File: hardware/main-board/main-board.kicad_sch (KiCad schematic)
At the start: 87 parts, among them J1 USB_C_Receptacle_USB2.0, J2 DNI, J3 Display Connector, J4 Conn_01x02, SW1 SW_Push, SW2 SW_Push, SW3 SW_Push, SW4 SW_Push, SW5 SW_Detect, SW6 SW_Boot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

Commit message: Various minor PCB fixups
Changed C1 footprint from an 0402 resistor to an 0402 capacitor. This
change shoulds be metadata only, or close to it, but makes the BOM data
less confusing.

Updated PCB metadata from schematic, which should pull in all of the BOM
manufacturer/vendor changes that were made when procuring components for
the production run.  It should also pull in any net name changes due to
KiCad updates.
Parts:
- C1: footprint Resistor_SMD:R_0402_1005Metric -> Capacitor_SMD:C_0402_1005Metric
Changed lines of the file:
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@@
     (property "Reference" "C1" (id 0) (at 27.94 24.6634 90))
     (property "Value" "1uF" (id 1) (at 27.94 26.9748 90))
-    (property "Footprint" "Resistor_SMD:R_0402_1005Metric" (id 2) (at 27.94 30.48 0)
+    (property "Footprint" "Capacitor_SMD:C_0402_1005Metric" (id 2) (at 27.94 30.48 0)
       (effects (font (size 1.27 1.27)) hide)
     )
@@
     )
     (path "/00000000-0000-0000-0000-00006056d7c9"
-      (reference "C1") (unit 1) (value "1uF") (footprint "Resistor_SMD:R_0402_1005Metric")
+      (reference "C1") (unit 1) (value "1uF") (footprint "Capacitor_SMD:C_0402_1005Metric")
     )
     (path "/00000000-0000-0000-0000-0000605786b2"

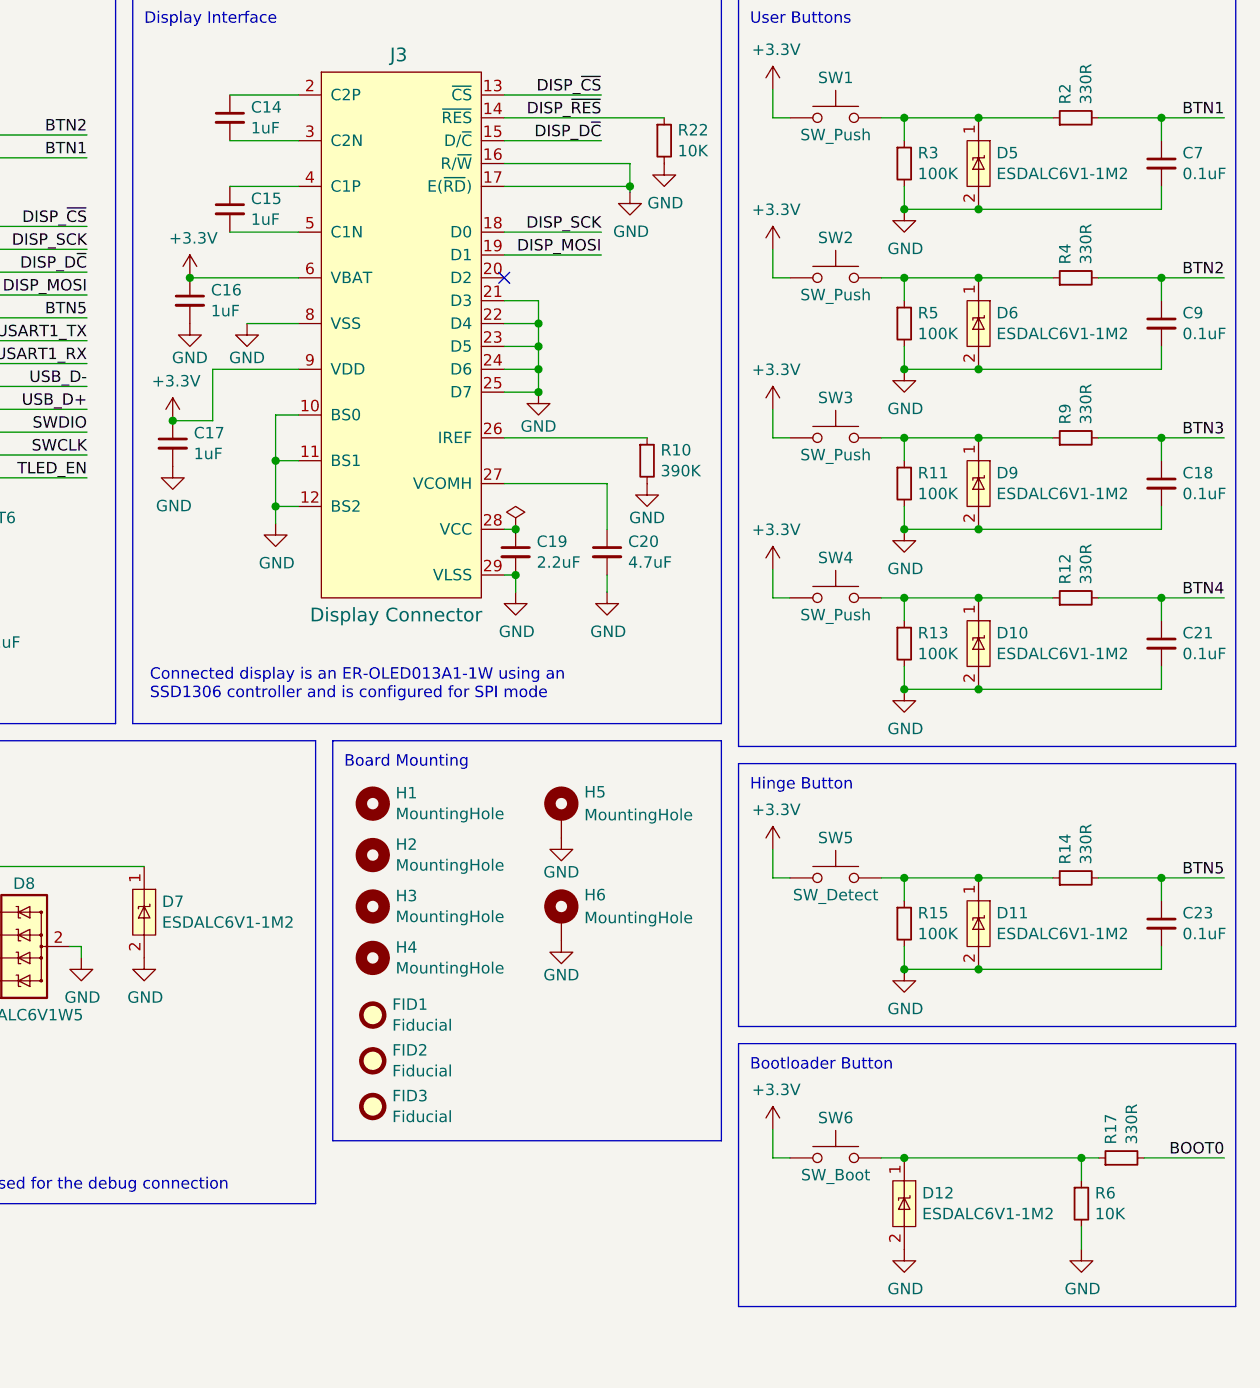
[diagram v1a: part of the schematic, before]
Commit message: Switch all single-line TVS diodes to the Semtech uClamp3301H
The ST diodes used in the original design had two main problems:
- Their package size made handling and manufacturability difficult,
  resulting in a lot of spotted issues on production boards
- Their rating can only protect 5V-tolerant lines, and a few of the
  buttons are actually connected on MCU pins that may only be 3.3V
  tolerant

This changes all of these diodes to a Semtech diode that's in a
larger and easier to handle package, which is also designed for
protecting 3.3V lines. Care was taken to minimize any and all changes
not strictly necessary for changing this one part, in an effort to
preserve the validity of existing EMC certification. That being said,
the only arcing ever seen during that testing was to the shield of the
USB connector, which is handled by completely unrelated protection
components.

If it is later determined that a TVS diode with a 5V working voltage is
more appropriate, Semtech also makes the uClamp0501H which is in an
identical package and can be a drop-in alternative.

Fix #41
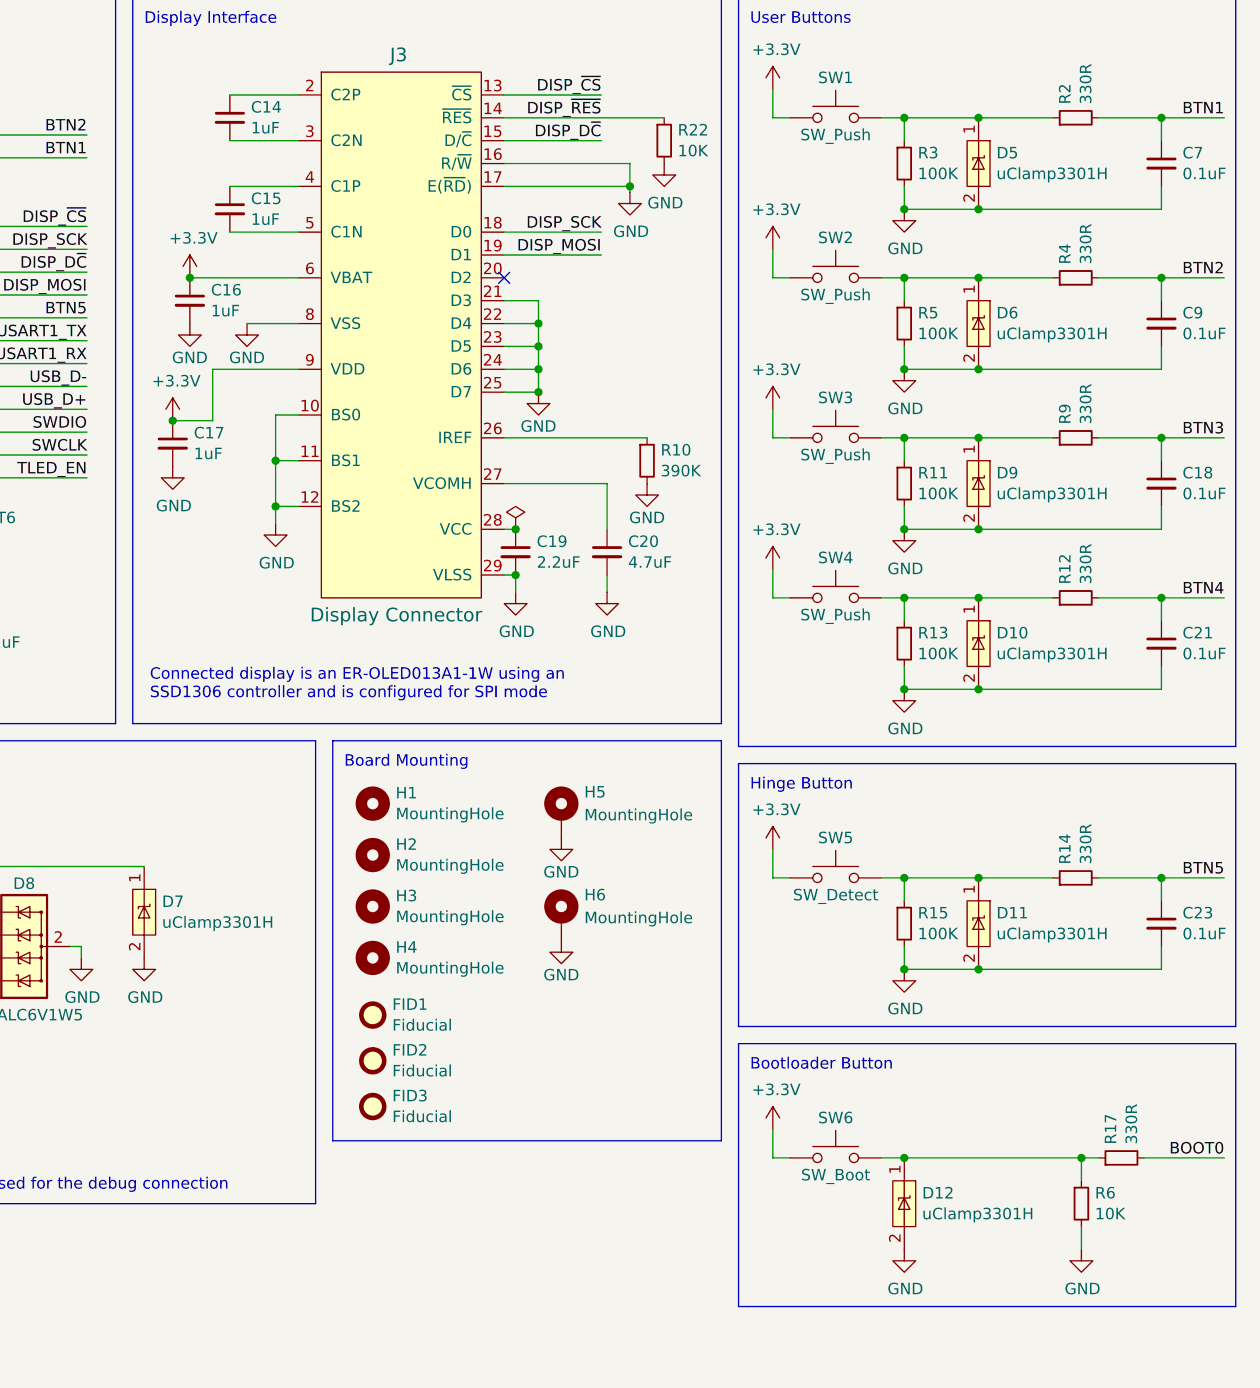
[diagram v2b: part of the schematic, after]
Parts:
- D10, D11, D12, D5, D6, D7, D9: value ESDALC6V1-1M2 -> uClamp3301H; footprint lib_fp:D_SOD-882 -> Diode_SMD:D_SOD-523; symbol Project:ESDALC6V1-1M2 -> Project:uClamp3301H; Manufacturer STMicroelectronics -> Semtech; Manufacturer PN ESDALC6V1-1M2 -> UCLAMP3301H.TCT; Supplier Mouser -> Digi-Key; Supplier PN 511-ESDALC6V1-1M2 -> UCLAMP3301HCT-ND

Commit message: Switch TVS diode from uClamp3301H to uClamp0501H
The 3301H has this annoying little feature called a snap-back voltage.
This means that if the voltage on the line ever exceeds the conservative
threshold of the diode, then it must fall below 2.8V before the diode
will stop conducting.

Given that transients associated with pushing a button will momentarily
exceed that threshold, this effectively results in a short across the
device's 3.3V power rail whenever a button is being held down. Thus, it
is safer to only protect buttons with TVS diodes that don't have this
feature.

Fix #41
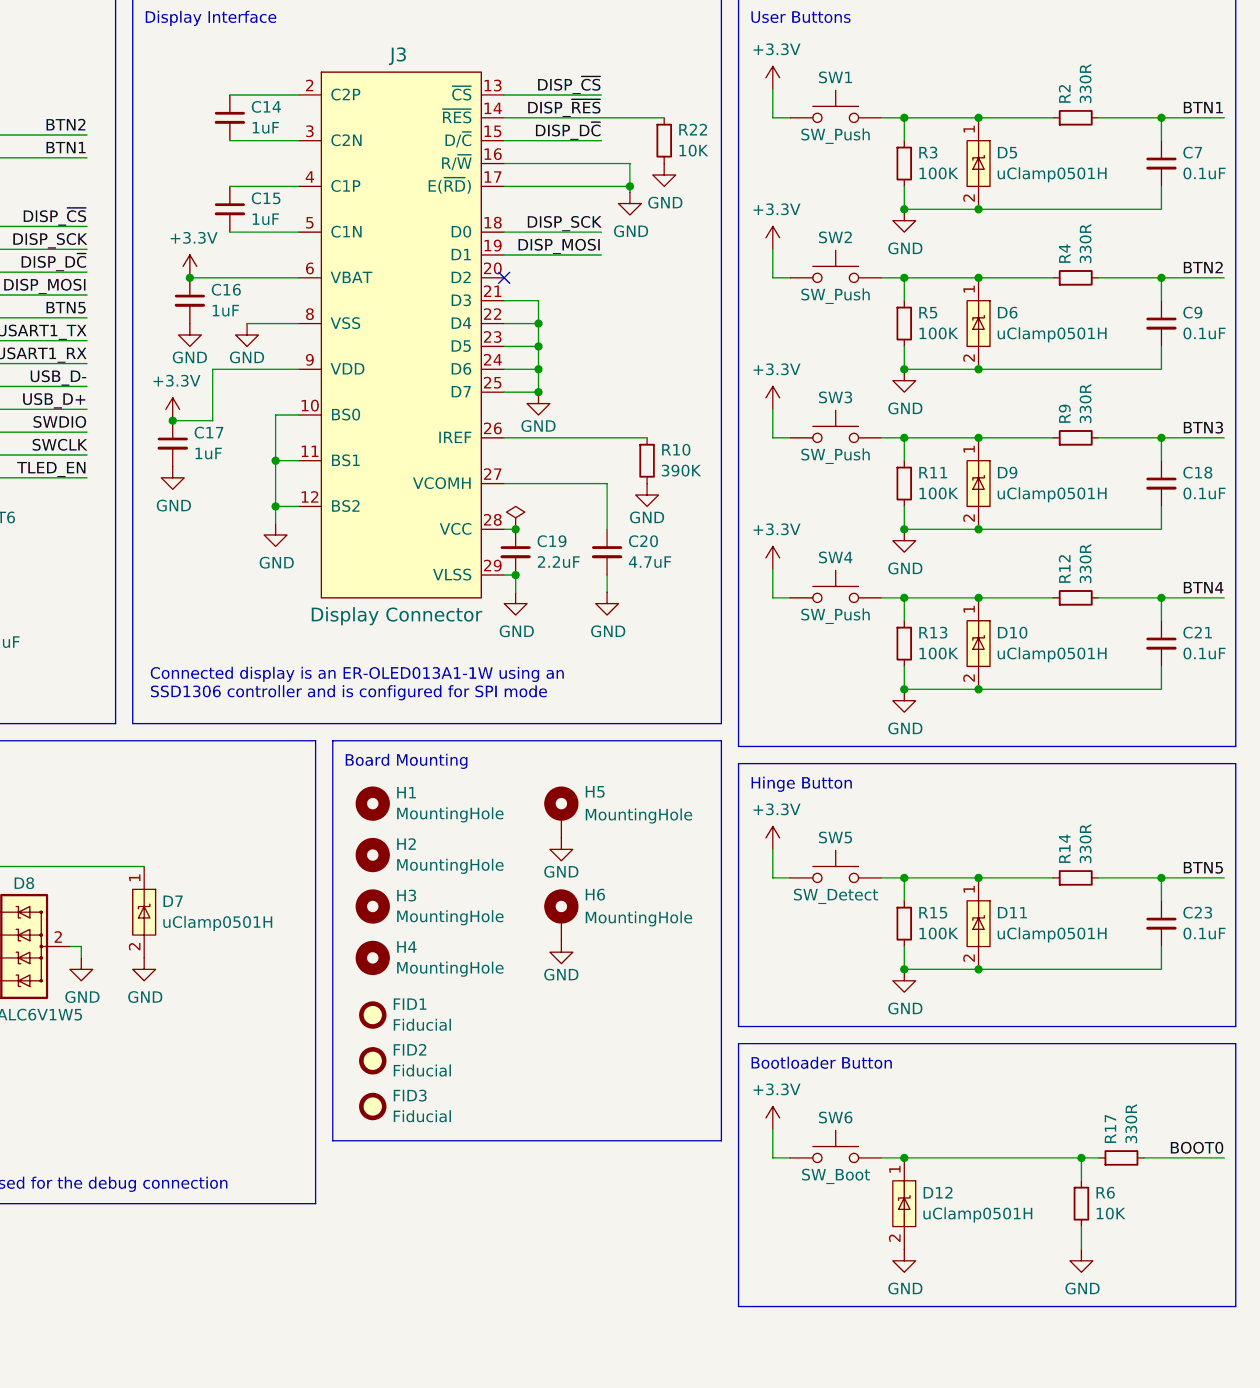
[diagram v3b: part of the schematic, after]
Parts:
- D10, D11, D12, D5, D6, D7, D9: value uClamp3301H -> uClamp0501H; Manufacturer PN UCLAMP3301H.TCT -> UCLAMP0501H.TCT; Supplier PN UCLAMP3301HCT-ND -> UCLAMP0501HCT-ND
